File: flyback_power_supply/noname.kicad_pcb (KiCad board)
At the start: 2 copper layers, 40.6 x 57.2 mm, 18 parts, among them J1 CONN_01X02, J2 CONN_01X02, T1 FlyBckTransformer, U1 LNK363D, U2 LTV-817

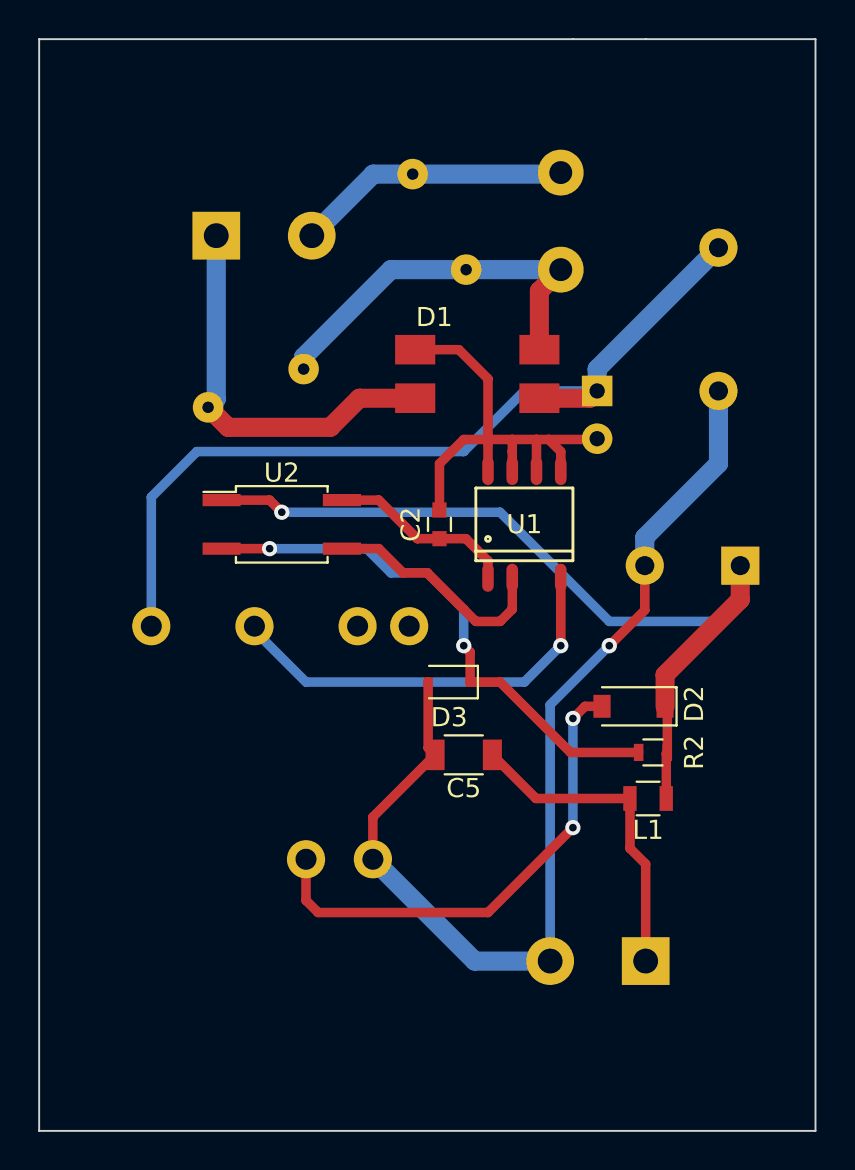
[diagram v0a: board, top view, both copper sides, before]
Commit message: Rerouted layout and added notes to front silk.
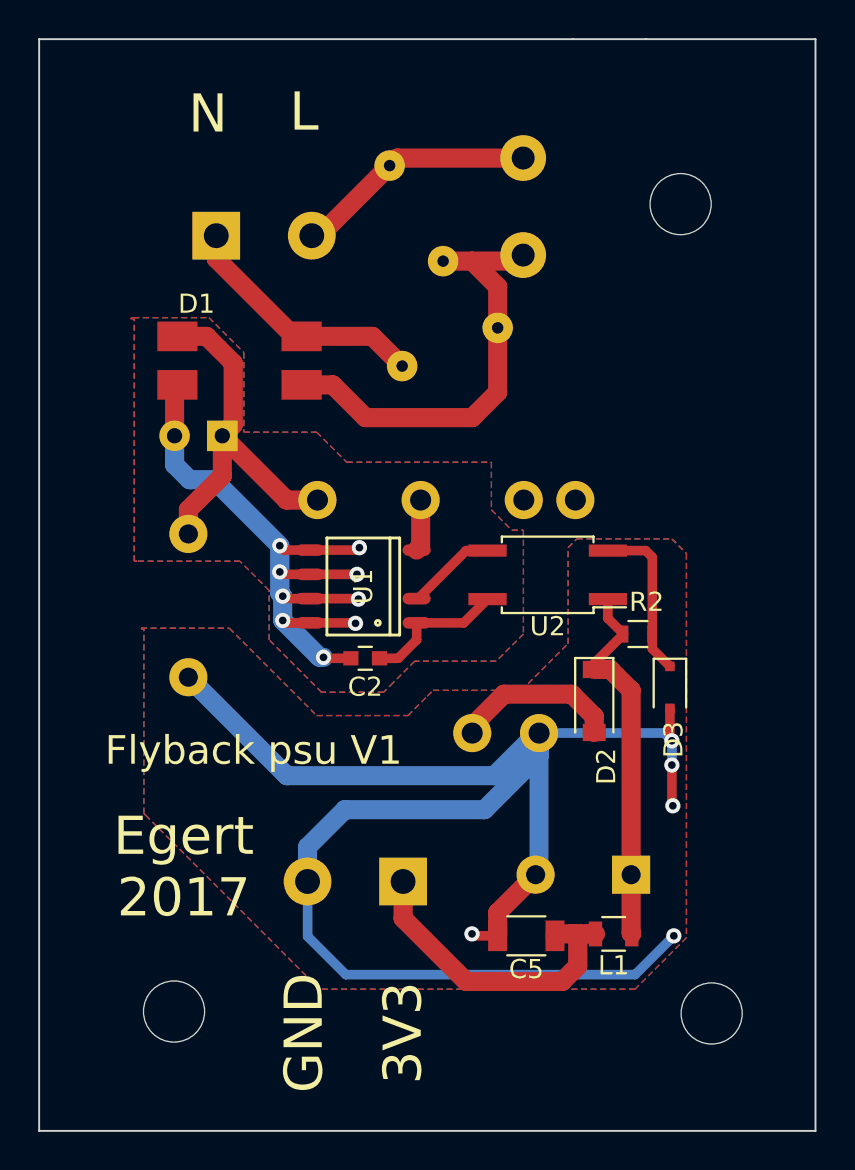
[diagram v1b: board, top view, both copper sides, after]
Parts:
- added REF**: MountingHole_3.2mm_M3, Mounting_Holes:MountingHole_3.2mm_M3, F.Cu at (187.6, 125.9)
- added REF**: MountingHole_3.2mm_M3, Mounting_Holes:MountingHole_3.2mm_M3, F.Cu at (159.5, 125.8)
- added REF**: MountingHole_3.2mm_M3, Mounting_Holes:MountingHole_3.2mm_M3, F.Cu at (186.0, 83.6)
- D1: value MB6S -> MB8S
- moved C3 31.5 mm to (160.2, 108.3)
- moved C1 19.8 mm to (162.0, 95.7), turned to 180 degrees
- moved C4 17.2 mm to (183.4, 118.7)
- moved U2 14.2 mm to (179.0, 103.0), turned to 180 degrees
- moved J2 13.4 mm to (171.4, 119.0)
- moved D1 12.5 mm to (159.6, 90.5)
- moved D3 11.6 mm to (185.4, 108.9), turned to 270 degrees
- moved T1 10.9 mm to (175.1, 105.2)
- moved RV1 10.4 mm to (176.4, 90.0)
- moved C5 10.0 mm to (177.9, 121.9)
- moved U1 9.04 mm to (169.4, 103.6), turned to 90 degrees
- moved C2 8.02 mm to (169.5, 107.3), turned to 180 degrees
- moved L1 7.31 mm to (182.5, 121.8)
- moved R2 6.25 mm to (183.7, 106.1), turned to 0 degrees
- moved R1 2.11 mm to (177.7, 86.2)
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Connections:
- D1 pad 1: GND -> /5
- D1 pad 2: /3 -> GND
- D1 pad 3: /5 -> /2
- D1 pad 4: /2 -> /3
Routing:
- net GNDA: track 55.8 -> 88.0 mm, vias 1 -> 5
- net Net-(C4-Pad1): track 45.9 -> 19.9 mm, vias 1 -> 0
- net /5: track 45.7 -> 19.8 mm
- net Net-(D3-Pad1): track 28.3 -> 8.57 mm, vias 2 -> 0
- net Net-(T1-Pad4): track 21.7 -> 2.71 mm, vias 1 -> 0
- net Net-(D2-Pad2): track 25.7 -> 8.79 mm, vias 2 -> 0
- net GND: track 25.7 -> 36.3 mm, vias 0 -> 9
- net Net-(U1-Pad2): track 12.4 -> 4.75 mm
- net /3: track 21.1 -> 13.6 mm
- net /2: track 20.6 -> 23.3 mm
- net Net-(C2-Pad1): track 9.85 -> 7.45 mm
- net /1: track 14.4 -> 12.7 mm
- net Net-(C5-Pad1): track 17.0 -> 17.5 mm
- added copper zone on B.Cu, net GND
- added copper zone on F.Cu, net GND
- added copper zone on B.Cu, net GNDA
- added copper zone on F.Cu, net GNDA
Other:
- board text added: "3V3"
- board text added: "Egert 2017"
- board text added: "Flyback psu V1"
- board text added: "GND"
- board text added: "L"
- board text added: "N"
